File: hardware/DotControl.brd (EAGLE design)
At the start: 30.7 x 65 mm, 44 parts, among them CN1 1X4-BIG, J3 USB-MICROB, SW2 Previous, SW5 Previous, SW6 Next, SW8 Ok, U1 ATMEGA328P-MU-QFN32, U2 TMP102, U3 ATSHA204-TSU, U4 SI7021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

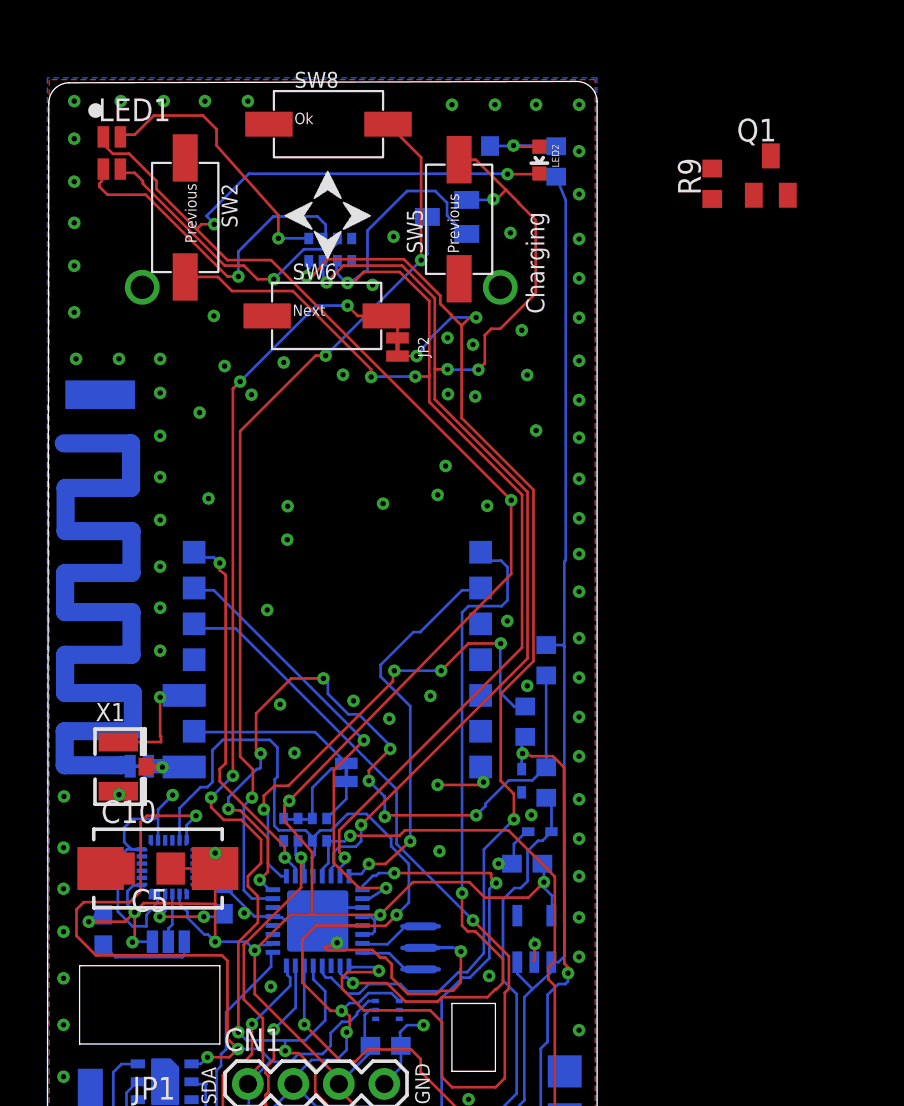
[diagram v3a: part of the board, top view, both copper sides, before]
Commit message: Replace LDO with low quiescence regulator
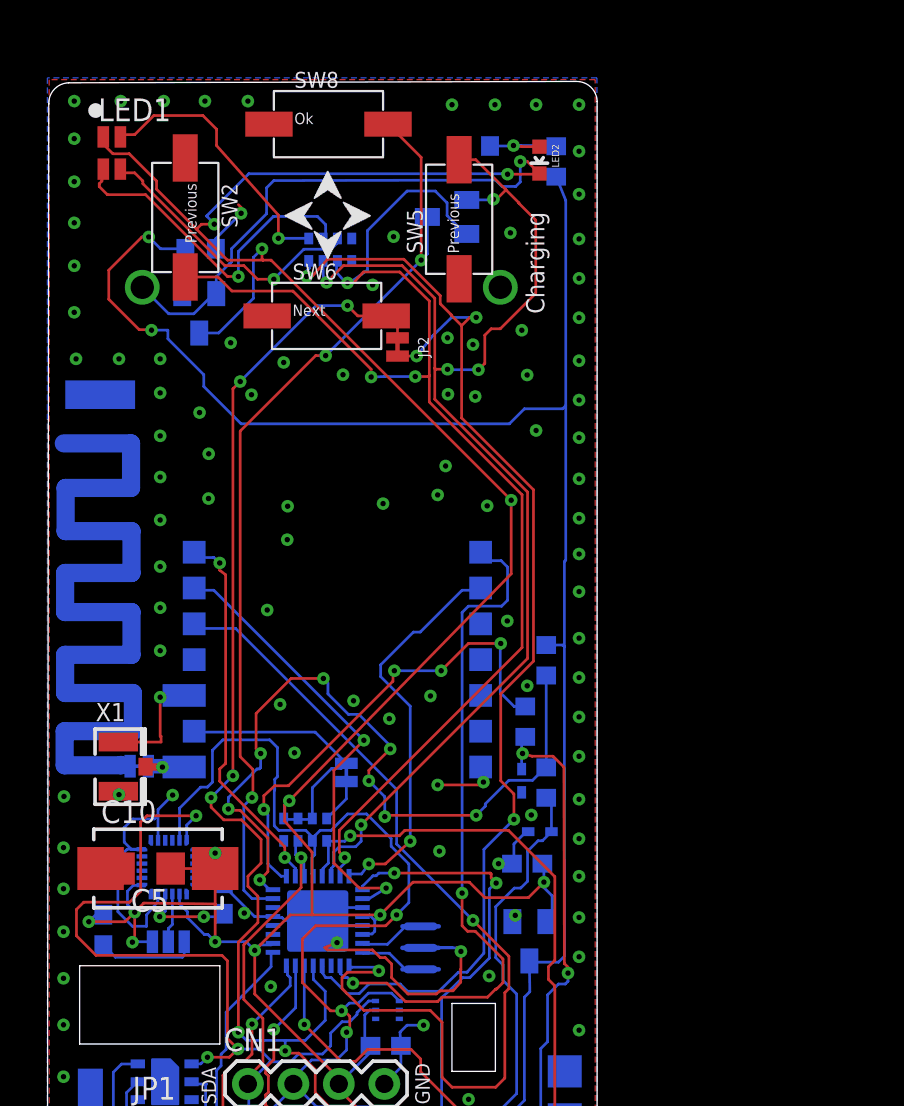
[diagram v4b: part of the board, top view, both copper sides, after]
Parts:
- removed U$4: LDCL015, LDCL015:SOT23-5
- added IC1: MCP1703CB, linear:SOT23
- moved Q1 32.8 mm to (8.48, 52.0), flipped to the bottom, turned to 180 degrees
- moved R9 28.8 mm to (8.56, 55.7), flipped to the bottom, turned to 0 degrees
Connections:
- net +3V3: now also IC1.2; no longer U$4.5
- net +5V: now also IC1.3; no longer U$4.1, U$4.3
- net GND: now also IC1.1; no longer U$4.2
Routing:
- net +5V: track 57.1 -> 95.1 mm, vias 0 -> 2
- net N$18: track 0.00 -> 29.4 mm, vias 0 -> 1
- net +3V3: track 217.6 -> 225.6 mm, vias 14 -> 15
- net GND: track 79.4 -> 79.7 mm, vias 105 -> 106

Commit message: Clean warnings
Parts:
- added C2: 1uF, rcl:C0603
- BAT1: value (none) -> 3V ML2032
- C1: value (none) -> 1uF
- D1, D2: value (none) -> MM5Z3V3
- R3, R4: value (none) -> 47Ω
- R5: value (none) -> 1.5kΩ
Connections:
- net +5V: now also C2.1
- net GND: now also C2.2
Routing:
- net GND: track 79.7 -> 90.8 mm, vias 106 -> 107
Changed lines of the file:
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@@
 <layer number="19" name="Unrouted" color="6" fill="1" visible="yes" active="yes"/>
 <layer number="20" name="Dimension" color="15" fill="1" visible="yes" active="yes"/>
-<layer number="21" name="tPlace" color="7" fill="1" visible="yes" active="yes"/>
-<layer number="22" name="bPlace" color="7" fill="1" visible="yes" active="yes"/>
+<layer number="21" name="tPlace" color="7" fill="1" visible="no" active="yes"/>
+<layer number="22" name="bPlace" color="7" fill="1" visible="no" active="yes"/>
 <layer number="23" name="tOrigins" color="15" fill="1" visible="yes" active="yes"/>
 <layer number="24" name="bOrigins" color="15" fill="1" visible="yes" active="yes"/>
@@
 <attribute name="PROD_ID" value="CONN-09505" x="28.9" y="5.7" size="1.778" layer="28" rot="MR270" display="off"/>
 </element>
-<element name="C1" library="rcl" package="C0603" value="" x="26.8" y="21.3" rot="MR0"/>
+<element name="C1" library="rcl" package="C0603" value="1uF" x="26.8" y="21.3" rot="MR0"/>
 <element name="JP3" library="adafruit" package="1X06" value="" x="15" y="2.1"/>
 <element name="U1" library="Seeed-OPL-ic" package="QFN32G-0.5-5X5MM" value="ATMEGA328P-MU-QFN32" x="15.1" y="18.1" rot="MR0">
@@
 <element name="SW2" library="Seeed-OPL-Switch" package="SW2-4.0-6.0X3.0X2.5MM" value="Previous" x="7.7" y="57.4" rot="R270"/>
 <element name="JP1" library="adafruit" package="1X08-CLEANBIG" value="" x="15" y="6.3"/>
-<element name="BAT1" library="Battery" package="BATTCOM_20MM_PTH" value="" x="25.3" y="53.5" rot="MR0"/>
+<element name="BAT1" library="Battery" package="BATTCOM_20MM_PTH" value="3V ML2032" x="25.3" y="53.5" rot="MR0"/>
 <element name="LED1" library="led" package="GM1WA55311A" value="GM1WA55311A" x="3.6" y="61"/>
 <element name="R2" library="SparkFun" package="0603-ARV" value="" x="15.8" y="55.6" rot="MR0"/>
@@
 </element>
 <element name="SJ2" library="SparkFun" package="SJ_2S-TRACE" value="SOLDERJUMPERTRACE" x="5.1308" y="26.7462" rot="MR0"/>
-<element name="D1" library="diode" package="SOD523" value="" x="27.559" y="23.0886" rot="MR0"/>
-<element name="D2" library="diode" package="SOD523" value="" x="26.4922" y="25.9842" rot="MR270"/>
-<element name="R3" library="rcl" package="R0603" value="" x="26.6954" y="29.2354" rot="MR90"/>
-<element name="R4" library="rcl" package="R0603" value="" x="27.8638" y="25.8318" rot="MR90"/>
-<element name="R5" library="rcl" package="R0603" value="" x="27.8638" y="32.6644" rot="MR90"/>
+<element name="D1" library="diode" package="SOD523" value="MM5Z3V3" x="27.559" y="23.0886" rot="MR0"/>
+<element name="D2" library="diode" package="SOD523" value="MM5Z3V3" x="26.4922" y="25.9842" rot="MR270"/>
+<element name="R3" library="rcl" package="R0603" value="47Ω" x="26.6954" y="29.2354" rot="MR90"/>
+<element name="R4" library="rcl" package="R0603" value="47Ω" x="27.8638" y="25.8318" rot="MR90"/>
+<element name="R5" library="rcl" package="R0603" value="1.5kΩ" x="27.8638" y="32.6644" rot="MR90"/>
 <element name="X1" library="adafruit" package="U.FL" value="" x="3.9624" y="26.7208"/>
 <element name="D4" library="diode" package="SOT23" value="BAS70-05" x="22.3266" y="57.4294" rot="MR270"/>
@@
 <element name="Q1" library="adafruit" package="SOT23" value="" x="8.4836" y="52.0446" rot="MR180"/>
 <element name="IC1" library="linear" package="SOT23" value="MCP1703CB" x="26.924" y="16.9672" rot="MR180"/>
+<element name="C2" library="rcl" package="C0603" value="1uF" x="27.9654" y="13.0302" rot="MR180"/>
 </elements>
 <signals>
@@
 <wire x1="10.8204" y1="57.6326" x2="10.8204" y2="57.9628" width="0.1524" layer="1"/>
 <wire x1="10.8204" y1="57.9628" x2="10.668" y2="58.1152" width="0.1524" layer="1"/>
+<wire x1="8.8" y1="63.9" x2="7.6454" y2="63.9" width="0.1524" layer="16"/>
+<wire x1="7.6454" y1="63.9" x2="7.6708" y2="59.5122" width="0.1524" layer="16"/>
+<via x="7.6708" y="59.5122" extent="1-16" drill="0.3"/>
+<wire x1="7.6708" y1="59.5122" x2="7.7" y2="62.1792" width="0.1524" layer="1"/>
+<wire x1="7.7" y1="62.1792" x2="7.7" y2="60.725" width="0.1524" layer="1"/>
+<contactref element="C2" pad="2"/>
+<wire x1="28.8154" y1="13.0302" x2="28.8154" y2="12.8846" width="0.1524" layer="16"/>
+<wire x1="28.8154" y1="12.8846" x2="29.7" y2="12" width="0.1524" layer="16"/>
 <wire x1="16.256" y1="17.85" x2="16.1798" y2="17.8308" width="0" layer="19" extent="16-16"/>
-<wire x1="7.7" y1="60.725" x2="8.8" y2="63.9" width="0" layer="19" extent="1-1"/>
 </signal>
 <signal name="SCK">
@@
 <wire x1="26.25" y1="7" x2="26.25" y2="7.6826" width="0.1524" layer="16"/>
 <wire x1="26.25" y1="7.6826" x2="26.6446" y2="8.0772" width="0.1524" layer="16"/>
-<wire x1="26.6446" y1="8.0772" x2="26.6446" y2="13.843" width="0.1524" layer="16"/>
+<wire x1="26.6446" y1="8.0772" x2="26.6446" y2="12.9794" width="0.1524" layer="16"/>
+<wire x1="26.6446" y1="13.0302" x2="26.6446" y2="13.843" width="0.1524" layer="16"/>
 <wire x1="26.6446" y1="13.843" x2="26.9494" y2="14.1478" width="0.1524" layer="16"/>
 <contactref element="R9" pad="2"/>
@@
 <via x="5.8166" y="51.1048" extent="1-16" drill="0.3"/>
 <wire x1="5.8166" y1="51.1048" x2="6.731" y2="51.1048" width="0.1524" layer="16"/>
+<contactref element="C2" pad="1"/>
+<wire x1="27.1154" y1="13.0302" x2="26.6446" y2="13.0302" width="0.1524" layer="16"/>
+<wire x1="26.6446" y1="13.0302" x2="26.6446" y2="12.9794" width="0.1524" layer="16"/>
 </signal>
 <signal name="MOSI">

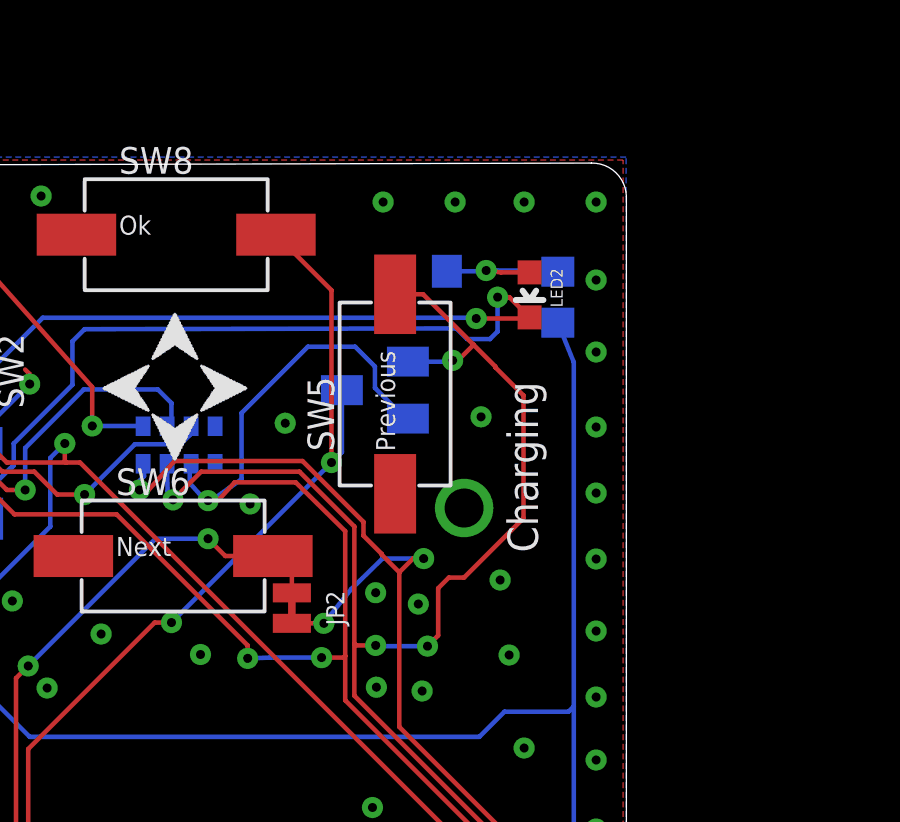
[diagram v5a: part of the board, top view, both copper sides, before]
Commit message: Improve GND, increase version
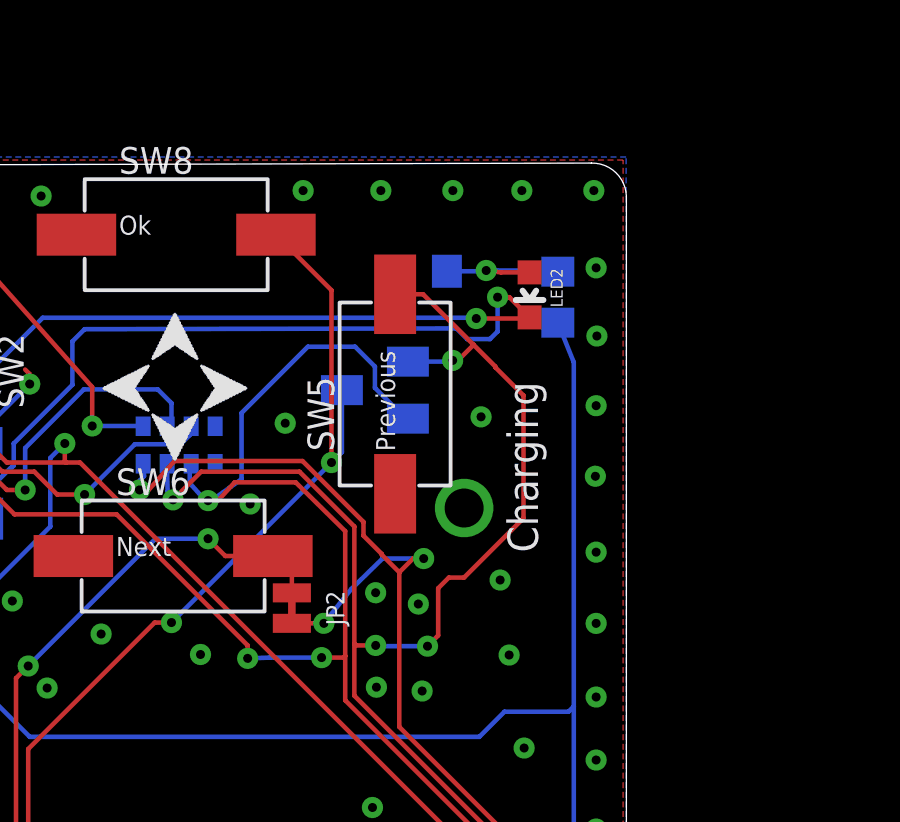
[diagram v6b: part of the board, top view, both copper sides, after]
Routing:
- net GND: vias 107 -> 108
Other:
- board text added: "DotControl v0.1.3"
- board text removed: "DotControl v0.1.2"
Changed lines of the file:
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@@
 <layer number="19" name="Unrouted" color="6" fill="1" visible="yes" active="yes"/>
 <layer number="20" name="Dimension" color="15" fill="1" visible="yes" active="yes"/>
-<layer number="21" name="tPlace" color="7" fill="1" visible="no" active="yes"/>
-<layer number="22" name="bPlace" color="7" fill="1" visible="no" active="yes"/>
+<layer number="21" name="tPlace" color="7" fill="1" visible="yes" active="yes"/>
+<layer number="22" name="bPlace" color="7" fill="1" visible="yes" active="yes"/>
 <layer number="23" name="tOrigins" color="15" fill="1" visible="yes" active="yes"/>
 <layer number="24" name="bOrigins" color="15" fill="1" visible="yes" active="yes"/>
@@
 <rectangle x1="14.8717" y1="41.9481" x2="15.0749" y2="41.9735" layer="22" rot="R180"/>
 <rectangle x1="12.9921" y1="41.9481" x2="14.1605" y2="41.9735" layer="22" rot="R180"/>
-<text x="28.0416" y="36.195" size="1.016" layer="22" font="vector" rot="MR270" align="center">DotControl v0.1.2</text>
+<text x="28.0416" y="36.195" size="1.016" layer="22" font="vector" rot="MR270" align="center">DotControl v0.1.3</text>
 <text x="6.477" y="2.1082" size="1.016" layer="21" font="vector" rot="R90" align="center">MOSI</text>
 <text x="23.4696" y="2.0828" size="1.016" layer="21" font="vector" rot="R90" align="center">GND</text>
@@
 <via x="29.7" y="45.1" extent="1-16" drill="0.3"/>
 <via x="29.7" y="47.2" extent="1-16" drill="0.3"/>
-<via x="29.7" y="49.4" extent="1-16" drill="0.3"/>
-<via x="29.7" y="51.8" extent="1-16" drill="0.3"/>
-<via x="29.7" y="54" extent="1-16" drill="0.3"/>
-<via x="29.7" y="56.2" extent="1-16" drill="0.3"/>
-<via x="29.7" y="58.7" extent="1-16" drill="0.3"/>
-<via x="29.7" y="61.1" extent="1-16" drill="0.3"/>
-<via x="29.7" y="63.7" extent="1-16" drill="0.3"/>
-<via x="27.3" y="63.7" extent="1-16" drill="0.3"/>
-<via x="25" y="63.7" extent="1-16" drill="0.3"/>
-<via x="22.6" y="63.7" extent="1-16" drill="0.3"/>
+<via x="29.7" y="49.654" extent="1-16" drill="0.3"/>
+<via x="29.7" y="52.0286" extent="1-16" drill="0.3"/>
+<via x="29.6746" y="54.5588" extent="1-16" drill="0.3"/>
+<via x="29.7" y="56.9112" extent="1-16" drill="0.3"/>
+<via x="29.7254" y="59.2334" extent="1-16" drill="0.3"/>
+<via x="29.7" y="61.5064" extent="1-16" drill="0.3"/>
+<via x="29.6238" y="64.081" extent="1-16" drill="0.3"/>
+<via x="27.2238" y="64.081" extent="1-16" drill="0.3"/>
+<via x="24.9238" y="64.081" extent="1-16" drill="0.3"/>
+<via x="22.5238" y="64.081" extent="1-16" drill="0.3"/>
 <via x="11.2" y="63.9" extent="1-16" drill="0.3"/>
 <via x="8.8" y="63.9" extent="1-16" drill="0.3"/>
@@
 <wire x1="28.8154" y1="13.0302" x2="28.8154" y2="12.8846" width="0.1524" layer="16"/>
 <wire x1="28.8154" y1="12.8846" x2="29.7" y2="12" width="0.1524" layer="16"/>
+<via x="19.933" y="64.081" extent="1-16" drill="0.3"/>
 <wire x1="16.256" y1="17.85" x2="16.1798" y2="17.8308" width="0" layer="19" extent="16-16"/>
 </signal>

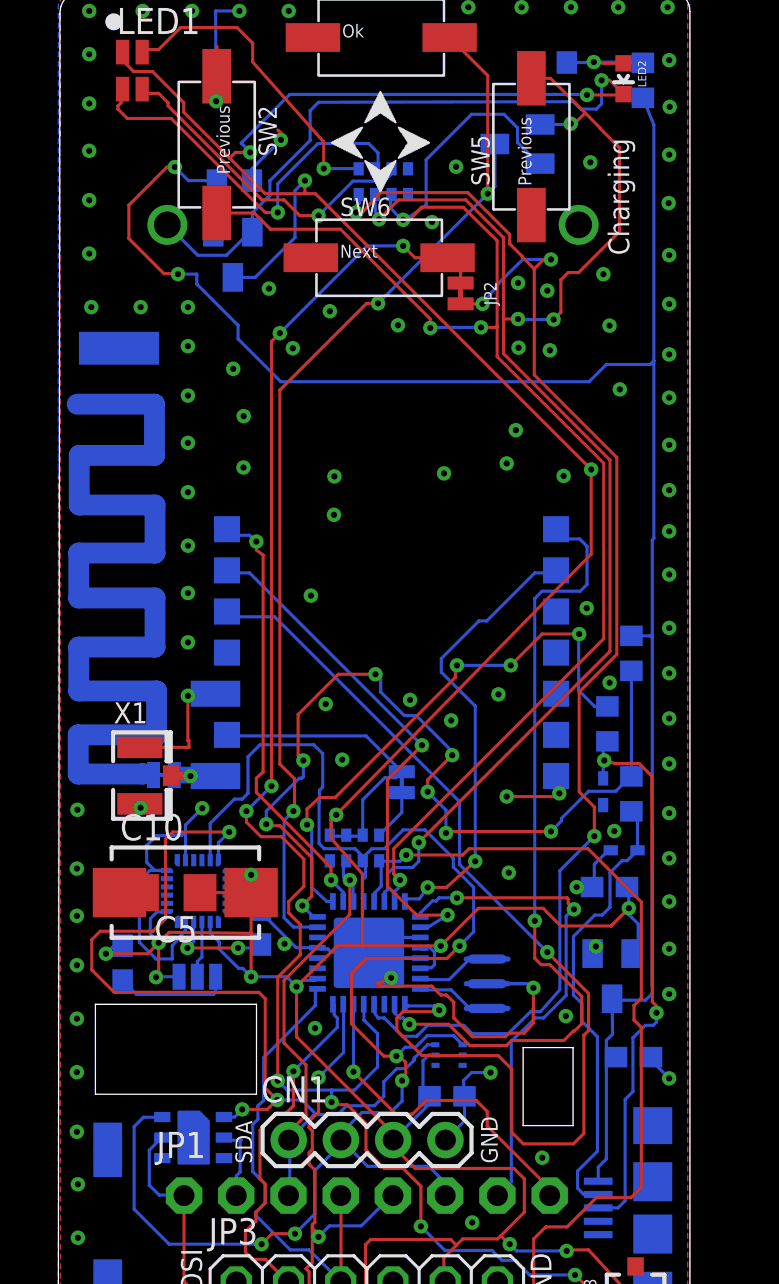
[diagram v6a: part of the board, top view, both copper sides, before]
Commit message: 2x100uF instead of 1x1000uF
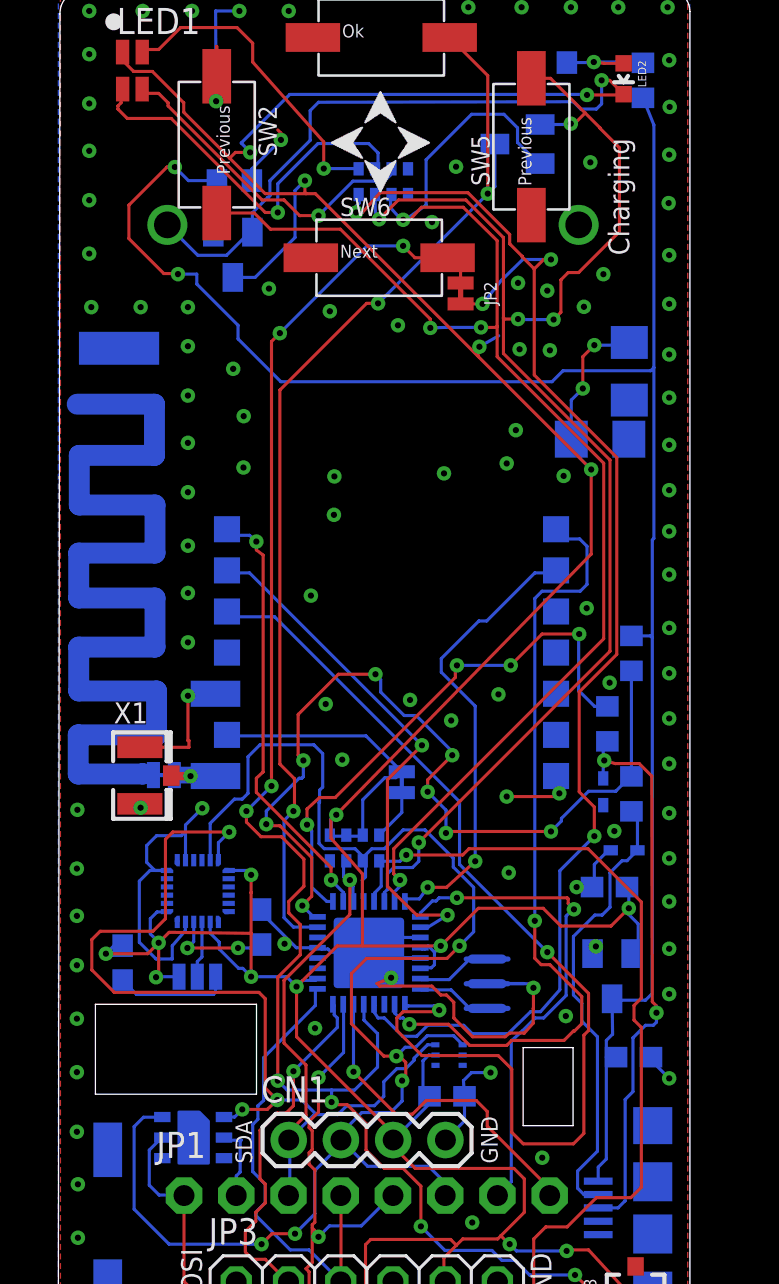
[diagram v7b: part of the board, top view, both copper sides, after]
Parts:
- removed C10: 1500uF 4V, adafruit:CT7343
- added C6: 100uF 4V, adafruit:C3216
- moved C5 30.3 mm to (26.3, 43.1), flipped to the bottom
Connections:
- net +3V3: now also C6.1; no longer C10.+
- net GND: now also C6.2; no longer C10.-
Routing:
- net +3V3: track 225.6 -> 232.5 mm, vias 15 -> 18
- net GND: vias 108 -> 106
